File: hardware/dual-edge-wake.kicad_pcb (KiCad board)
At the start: 2 copper layers, 28.7 x 22.1 mm, 17 parts, among them J1 Conn_01x04_Male, J2 Circuit, J3 Falling, J4 Leading, Q1 BC807, Q2 BC847, Q3 BC847, U1 SN74LVC1G86DBVR

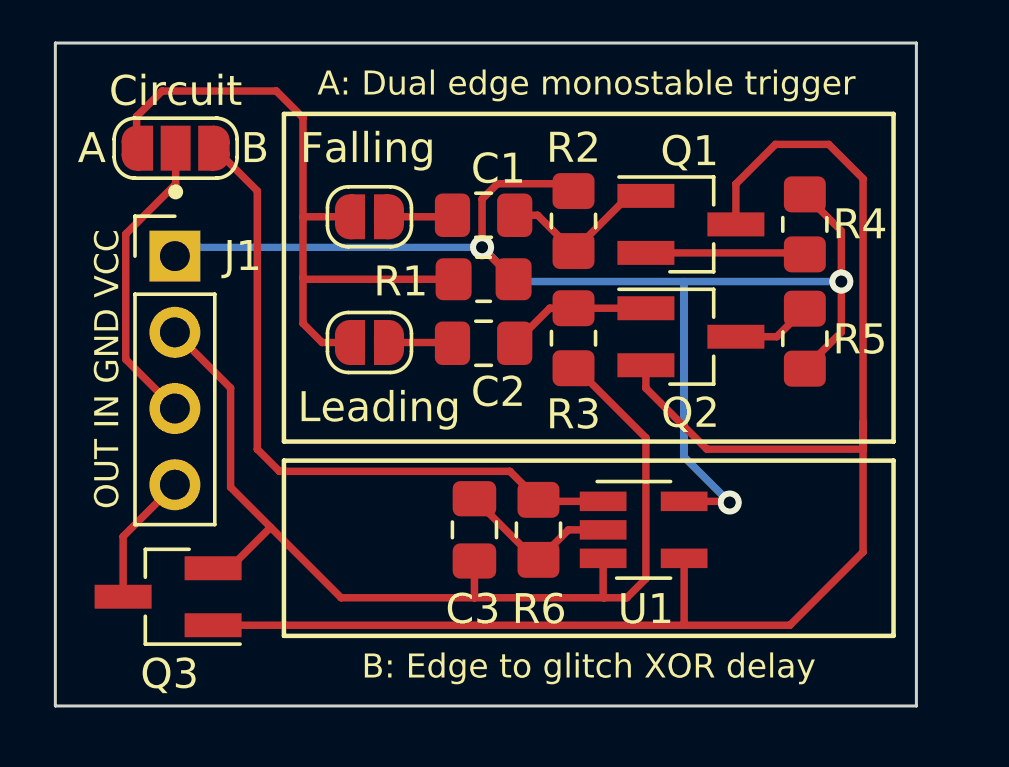
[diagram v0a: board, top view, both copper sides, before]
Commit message: Fixed #2
Add resistor between circuit outputs, removed pull-up on circuit A input. Also add rear SS
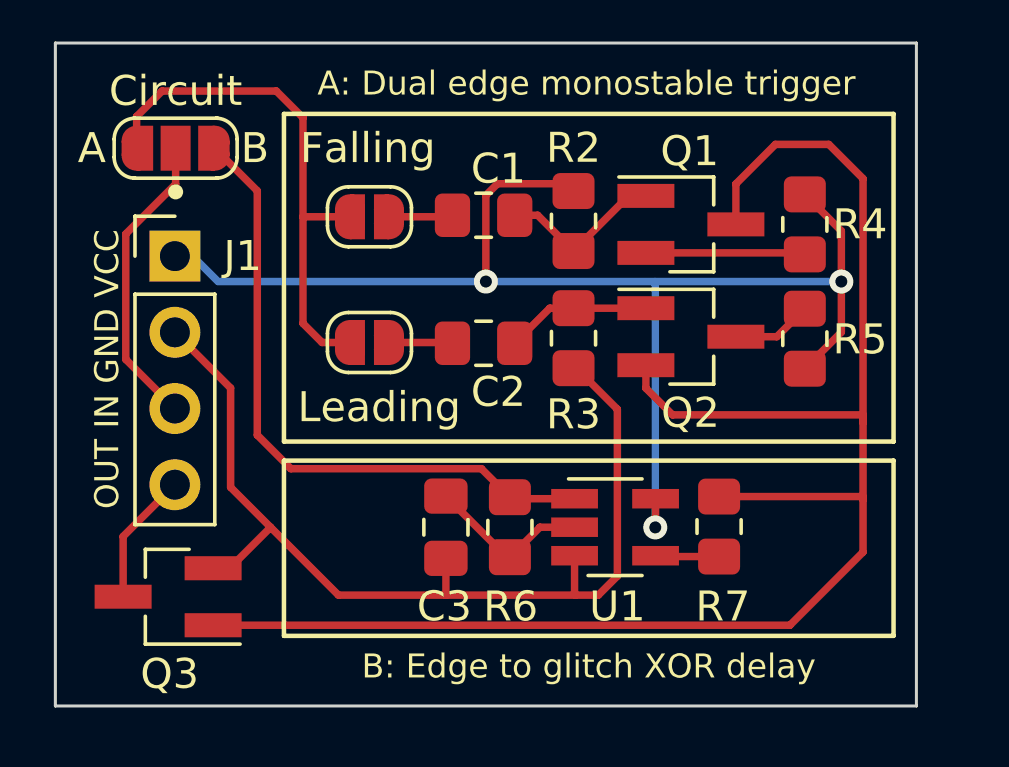
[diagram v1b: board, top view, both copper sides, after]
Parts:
- removed R1: 100k, Resistor_SMD:R_0805_2012Metric_Pad1.20x1.40mm_HandSolder
- added R7: 1k, Resistor_SMD:R_0805_2012Metric_Pad1.20x1.40mm_HandSolder, F.Cu at (113.5, 64.2)
- moved C3 0.96 mm to (104.4, 64.2)
- moved R6 0.96 mm to (106.5, 64.2)
- moved U1 0.96 mm to (110.0, 64.2)
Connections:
- U1 pad 4: /C -> Net-(U1-Pad4)
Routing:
- net /A: track 22.6 -> 17.6 mm
- net Net-(U1-Pad4): track 0.00 -> 2.09 mm
- net GND: track 34.0 -> 32.6 mm
- net /C: track 53.7 -> 55.2 mm
- net /B: track 22.8 -> 21.5 mm
- net +3.3V: track 44.9 -> 44.1 mm
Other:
- board text added: "Input: Use 100k pull up/down Output: Open collector BC847"
- board text added: "Nick Bolton ESP8266 dual edge wake Rev 1b"
- board text added: "github.com/nbolton/esp8266-dual-edge-wake"

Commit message: Tidied up SS, updated rev
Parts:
- moved C1 0.95 mm to (106.6, 54.0), turned to -90 degrees
- moved C2 0.94 mm to (106.6, 57.9), turned to 90 degrees
- moved J3 0.54 mm to (102.4, 53.8)
- moved J4 0.54 mm to (102.4, 58.0)
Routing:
- net Net-(C1-Pad1): track 2.07 -> 3.91 mm
- net Net-(C2-Pad1): track 2.09 -> 3.92 mm
- net /A: track 17.6 -> 18.7 mm
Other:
- board size 28.7 x 22.1 mm -> 28.1 x 22.1 mm

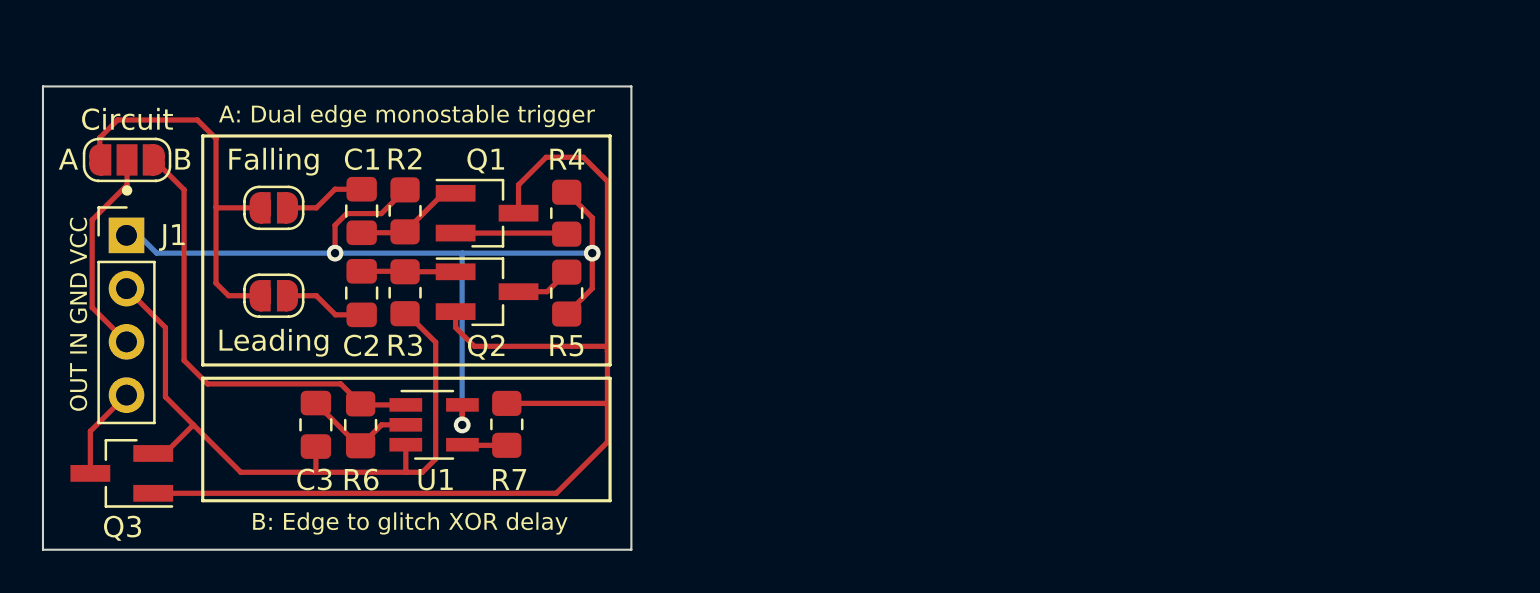
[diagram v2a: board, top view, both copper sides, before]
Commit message: WIP - Add pull ups and LEDs
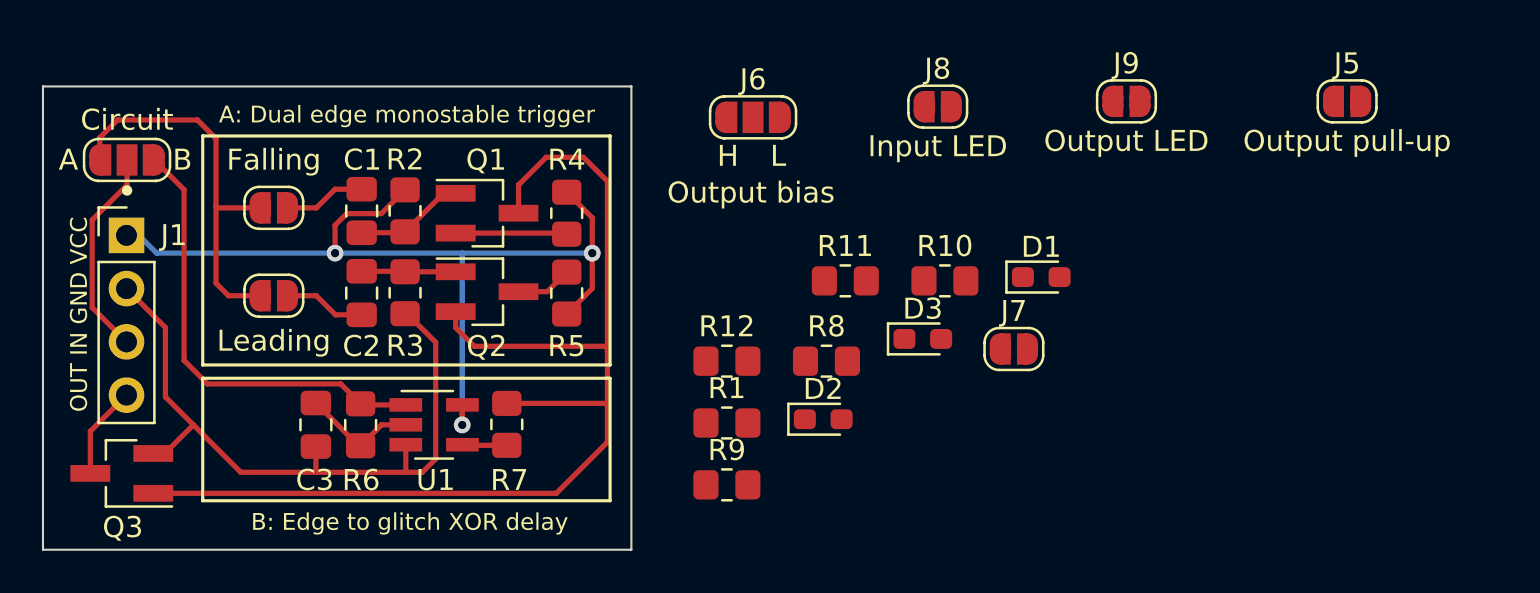
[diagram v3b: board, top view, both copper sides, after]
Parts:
- added D1: LED, LED_SMD:LED_0603_1608Metric_Pad1.05x0.95mm_HandSolder, F.Cu at (139.0, 57.1)
- added D2: LED, LED_SMD:LED_0603_1608Metric_Pad1.05x0.95mm_HandSolder, F.Cu at (128.6, 63.9)
- added D3: LED, LED_SMD:LED_0603_1608Metric_Pad1.05x0.95mm_HandSolder, F.Cu at (133.3, 60.1)
- added J5: Output pull-up, Jumper:SolderJumper-2_P1.3mm_Open_RoundedPad1.0x1.5mm, F.Cu at (153.6, 48.8)
- added J6: Output bias, Nick:SolderJumper-3_HL, F.Cu at (125.2, 49.5)
- added J7: Vcc LED, Jumper:SolderJumper-2_P1.3mm_Open_RoundedPad1.0x1.5mm, F.Cu at (137.7, 60.6)
- added J8: Input LED, Jumper:SolderJumper-2_P1.3mm_Open_RoundedPad1.0x1.5mm, F.Cu at (134.0, 49.0)
- added J9: Output LED, Jumper:SolderJumper-2_P1.3mm_Open_RoundedPad1.0x1.5mm, F.Cu at (143.0, 48.8)
- added R1: 100k, Resistor_SMD:R_0805_2012Metric_Pad1.20x1.40mm_HandSolder, F.Cu at (124.0, 64.1)
- added R10: 10k, Resistor_SMD:R_0805_2012Metric_Pad1.20x1.40mm_HandSolder, F.Cu at (134.4, 57.3)
- added R11: 10k, Resistor_SMD:R_0805_2012Metric_Pad1.20x1.40mm_HandSolder, F.Cu at (129.6, 57.3)
- added R12: 10k, Resistor_SMD:R_0805_2012Metric_Pad1.20x1.40mm_HandSolder, F.Cu at (124.0, 61.2)
- added R8: 100k, Resistor_SMD:R_0805_2012Metric_Pad1.20x1.40mm_HandSolder, F.Cu at (128.7, 61.2)
- added R9: 100k, Resistor_SMD:R_0805_2012Metric_Pad1.20x1.40mm_HandSolder, F.Cu at (124.0, 67.1)
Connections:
- net +3.3V renamed +5V

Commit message: Add todo to PCB
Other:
- board text added: "TODO: Put jumpers on back of module"
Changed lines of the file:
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@@
+    (effects (font (size 1 1) (thickness 0.15)))
+  )
+  (gr_text "TODO: Put jumpers on back of module" (at 104.902 45.72) (layer "Cmts.User")
     (effects (font (size 1 1) (thickness 0.15)))
   )

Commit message: Add input resistor
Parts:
- added R13: 100k, Resistor_SMD:R_0805_2012Metric_Pad1.20x1.40mm_HandSolder, F.Cu at (147.5, 58.5)
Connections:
- J1 pad 3: /Input -> Net-(J1-Pin_3)
